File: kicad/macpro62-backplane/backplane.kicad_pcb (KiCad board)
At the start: 6 copper layers, 122 x 122 mm, 29 parts, among them J1 CPU-LINK: Amphenol Mini Cool 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, J10 MCIO 124 RA OUT -> Face S (x4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, J2 PSU-IN: Micro-Fit 3.0 2x4 (12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, J3 FACE-P AUX: JST GH 15P (MP62-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, J4 FACE-S AUX: JST GH 15P (same 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, J6 IOB-LINK: GH 15P <-> IOB J6 (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, J7 OpenCore boot: M.2 M-key sock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, J8 SWD (3V3, SWCLK, SWDIO, GND) 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, J9 MCIO 124 RA OUT -> Face P (x1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, SW1 BOOTSEL (fp5: PSU side), SW2 Bench power button, U1 RP2350A (LCSC C42411118), U10 OPTION Gen5: DS320PR810 #1, F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, U11 OPTION Gen5: DS320PR810 #2, F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, U12 OPTION Gen5: DS320PR810 #3, F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, U13 OPTION Gen5: DS320PR810 #4, F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, U14 OPTION Gen5: DS320PR810 #5, F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, U2 W25Q128 QSPI flash (part TBD), U3 TMP1075 core-base temp sensor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, U4 TMP1075 PSU-side temp sensor 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, Y1 12 MHz crystal

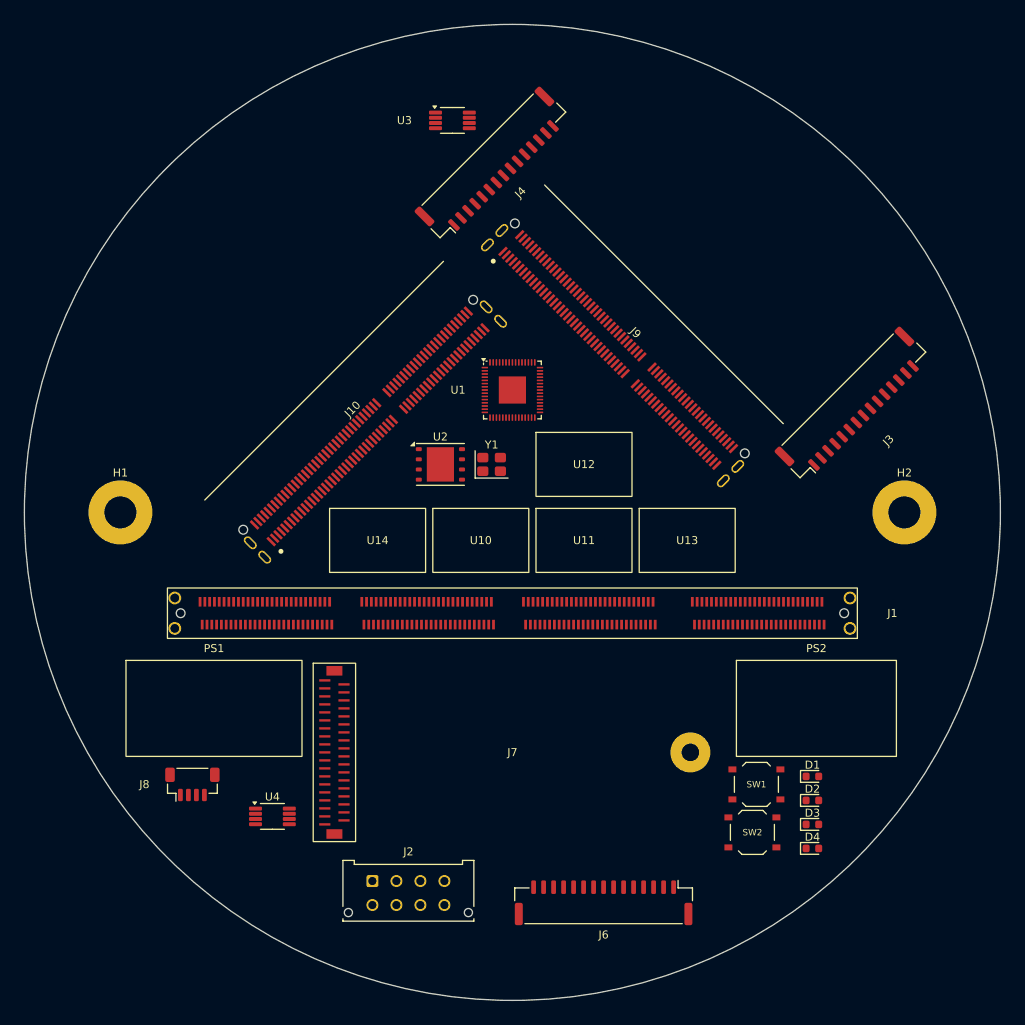
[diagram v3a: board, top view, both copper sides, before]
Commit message: Backplane rev A1: 4-layer JLC04161H-7628, Gen5 redrivers removed, RP2350B MCU + INA226, fully routed (DRC/ERC 0, all HS/SATA pairs 0 skew), USB2 skew touch-up, JLC outputs
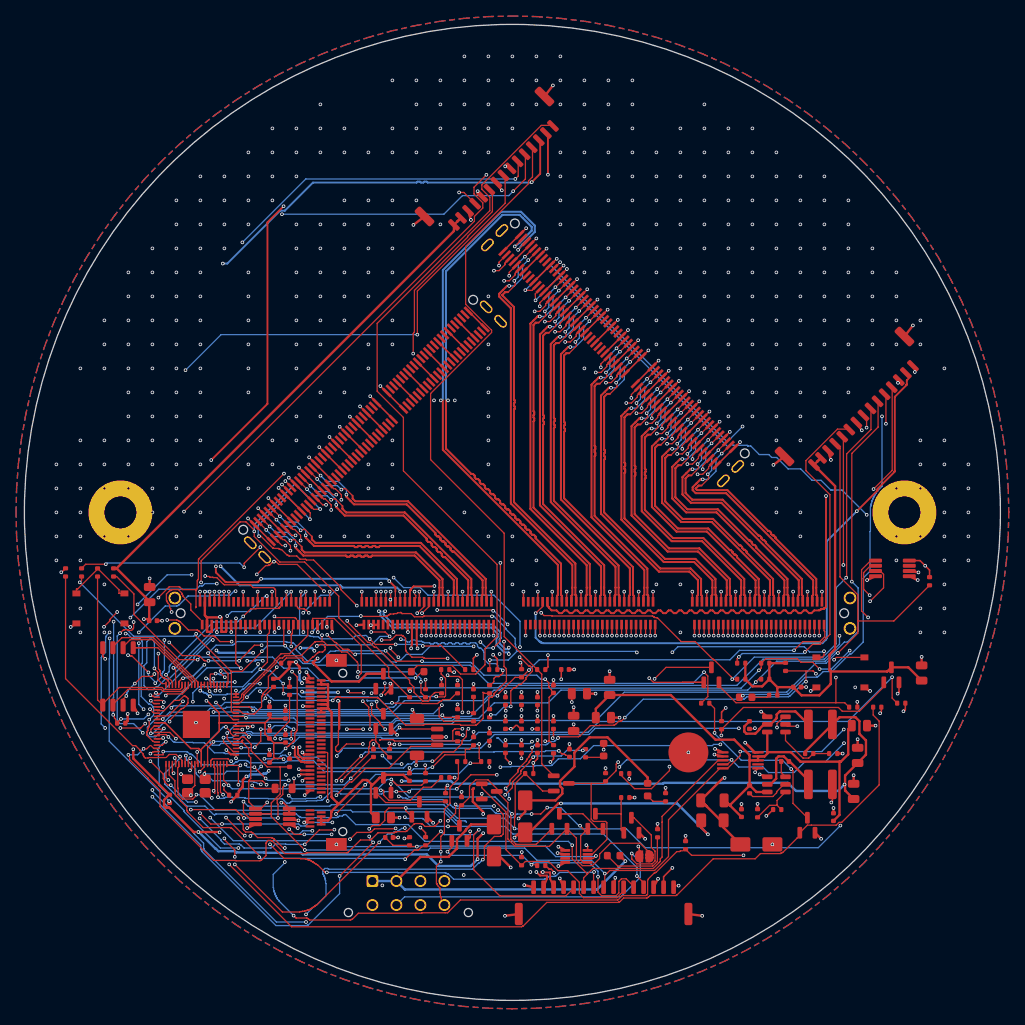
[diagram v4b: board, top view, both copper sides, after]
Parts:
- removed PS1: Standby power + HW safety gate, MP62_Placeholders:MP62_AREA_StandbyPower_22x12_PLACEHOLDER
- removed PS2: Main-rail power (3V3_BP incl. redrivers ~6.5 W), MP62_Placeholders:MP62_AREA_MainPower_20x12_PLACEHOLDER
- removed U10: OPTION Gen5: DS320PR810 #1, Face P lanes 0-3 (TX+RX), MP62_Placeholders:MP62_AREA_Redriver_DS320PR810_12x8_PLACEHOLDER
- removed U11: OPTION Gen5: DS320PR810 #2, Face P lanes 4-7 (TX+RX), MP62_Placeholders:MP62_AREA_Redriver_DS320PR810_12x8_PLACEHOLDER
- removed U12: OPTION Gen5: DS320PR810 #3, Face P lanes 8-11 (TX+RX), MP62_Placeholders:MP62_AREA_Redriver_DS320PR810_12x8_PLACEHOLDER
- removed U13: OPTION Gen5: DS320PR810 #4, Face P lanes 12-15 (TX+RX), MP62_Placeholders:MP62_AREA_Redriver_DS320PR810_12x8_PLACEHOLDER
- removed U14: OPTION Gen5: DS320PR810 #5, Face S lanes 0-3 (TX+RX), MP62_Placeholders:MP62_AREA_Redriver_DS320PR810_12x8_PLACEHOLDER
- added C1: 100nF 16V X7R 0402, MP62_BP:C_0402_1005Metric, F.Cu at (147.1, 128.1)
- added C10: 22uF 25V X5R 0805, MP62_BP:C_0805_2012Metric, F.Cu at (192.7, 134.9)
- added C11: 22uF 25V X5R 0805, MP62_BP:C_0805_2012Metric, F.Cu at (193.2, 130.4)
- added C12: 100nF 16V X7R 0402, MP62_BP:C_0402_1005Metric, F.Cu at (178.6, 137.6)
- added C13: 22uF 25V X5R 0805, MP62_BP:C_0805_2012Metric, F.Cu at (201.2, 120.1)
- added C14: 100nF 16V X7R 0402, MP62_BP:C_0402_1005Metric, F.Cu at (185.6, 121.8)
- added C15: 22uF 25V X5R 0805, MP62_BP:C_0805_2012Metric, F.Cu at (104.7, 110.3)
- added C16: 100nF 16V X7R 0402, MP62_BP:C_0402_1005Metric, F.Cu at (105.1, 113.5)
- added C17: 22uF 25V X5R 0805, MP62_BP:C_0805_2012Metric, F.Cu at (133.9, 138.2)
- added C18: 100nF 16V X7R 0402, MP62_BP:C_0402_1005Metric, F.Cu at (137.1, 133.1)
- added C19: 100nF 16V X7R 0402, MP62_BP:C_0402_1005Metric, F.Cu at (149.1, 126.6)
- added C2: 22uF 25V X5R 0805, MP62_BP:C_0805_2012Metric, F.Cu at (193.4, 126.7)
- added C20: 1uF 25V X5R 0402, MP62_BP:C_0402_1005Metric, F.Cu at (134.6, 140.6)
- added C21: 100nF 16V X7R 0402, MP62_BP:C_0402_1005Metric, F.Cu at (149.1, 123.6)
- added C22: 100nF 16V X7R 0402, MP62_BP:C_0402_1005Metric, F.Cu at (149.1, 129.6)
- added C23: 100nF 16V X7R 0402, MP62_BP:C_0402_1005Metric, F.Cu at (151.1, 126.6)
- added C24: 100nF 16V X7R 0402, MP62_BP:C_0402_1005Metric, F.Cu at (151.1, 123.6)
- added C25: 100nF 16V X7R 0402, MP62_BP:C_0402_1005Metric, F.Cu at (151.1, 129.6)
- added C26: 100nF 16V X7R 0402, MP62_BP:C_0402_1005Metric, F.Cu at (153.1, 126.6)
- added C27: 100nF 16V X7R 0402, MP62_BP:C_0402_1005Metric, F.Cu at (153.1, 123.6)
- added C28: 100nF 16V X7R 0402, MP62_BP:C_0402_1005Metric, F.Cu at (153.1, 129.6)
- added C29: 4.7uF 10V X5R 0402, MP62_BP:C_0402_1005Metric, F.Cu at (155.1, 126.6)
- added C3: 22uF 25V X5R 0805, MP62_BP:C_0805_2012Metric, F.Cu at (161.4, 125.7)
- added C30: 4.7uF 10V X5R 0402, MP62_BP:C_0402_1005Metric, F.Cu at (119.6, 127.8)
- added C31: 4.7uF 10V X5R 0402, MP62_BP:C_0402_1005Metric, F.Cu at (119.6, 130.8)
- added C32: 100nF 16V X7R 0402, MP62_BP:C_0402_1005Metric, F.Cu at (119.6, 124.8)
- added C33: 100nF 16V X7R 0402, MP62_BP:C_0402_1005Metric, F.Cu at (121.6, 128.3)
- added C34: 100nF 16V X7R 0402, MP62_BP:C_0402_1005Metric, F.Cu at (121.6, 125.3)
- added C35: 100nF 16V X7R 0402, MP62_BP:C_0402_1005Metric, F.Cu at (155.1, 122.1)
- added C36: 15pF 50V C0G 0402, MP62_BP:C_0402_1005Metric, F.Cu at (132.6, 130.1)
- added C37: 15pF 50V C0G 0402, MP62_BP:C_0402_1005Metric, F.Cu at (145.1, 122.6)
- added C38: 100nF 16V X7R 0402, MP62_BP:C_0402_1005Metric, F.Cu at (156.6, 119.6)
- added C39: 100nF 16V X7R 0402, MP62_BP:C_0402_1005Metric, F.Cu at (157.1, 130.1)
- added C4: 22uF 25V X5R 0805, MP62_BP:C_0805_2012Metric, F.Cu at (162.2, 121.9)
- added C5: 100nF 16V X7R 0402, MP62_BP:C_0402_1005Metric, F.Cu at (184.1, 131.1)
- added C6: 22uF 25V X5R 0805, MP62_BP:C_0805_2012Metric, F.Cu at (157.7, 126.4)
- added C7: 22uF 25V X5R 0805, MP62_BP:C_0805_2012Metric, F.Cu at (158.4, 122.7)
- added C8: 100nF 16V X7R 0402, MP62_BP:C_0402_1005Metric, F.Cu at (190.1, 138.1)
- added C9: 100nF 16V X7R 0402, MP62_BP:C_0402_1005Metric, F.Cu at (179.6, 126.6)
- added D10: LED red 0603, MP62_BP:LED_0603_1608Metric, F.Cu at (161.4, 129.7)
- added D5: BAT54A (LBAT54ALT1G), MP62_BP:SOT-23, F.Cu at (156.1, 133.9)
- added D6: LED red 0603, MP62_BP:LED_0603_1608Metric, F.Cu at (179.2, 123.1)
- added D7: LED red 0603, MP62_BP:LED_0603_1608Metric, F.Cu at (138.2, 119.9)
- added D8: LED red 0603, MP62_BP:LED_0603_1608Metric, F.Cu at (162.7, 142.9)
- added D9: LED red 0603, MP62_BP:LED_0603_1608Metric, F.Cu at (166.9, 134.7)
- added F1: 3A 1206 fast fuse (0466003.NRHF class), MP62_BP:Fuse_1206_3216Metric, F.Cu at (175.0, 138.5)
- added H3: M.2 2242 standoff pad (DNP option), MP62_BP:MP62_M2_Standoff_SMT_M2_Pad5.0, F.Cu at (172.0, 130.0)
- added JP1: BENCH: bridges the Hall interlock (open = normal), MP62_BP:SolderJumper-2_P1.3mm_Open_RoundedPad1.0x1.5mm, F.Cu at (166.5, 143.0)
- added L1: 4.7uH 2A 4x4 (SWPA4030S4R7MT), MP62_BP:L_Changjiang_FNR4030S, F.Cu at (188.5, 134.0)
- added L2: 4.7uH 2A 4x4 (SWPA4030S4R7MT), MP62_BP:L_Changjiang_FNR4030S, F.Cu at (188.5, 126.5)
- added L3: 3.3uH 0806 (FNR201610S3R3MT, RP2350 VREG), MP62_BP:L_0805_2012Metric, F.Cu at (121.4, 134.5)
- added Q1: AO3401A P-MOS, MP62_BP:SOT-23, F.Cu at (197.4, 120.3)
- added Q10: 2N7002 N-MOS, MP62_BP:SOT-23, F.Cu at (186.9, 139.1)
- added Q11: 2N7002 N-MOS, MP62_BP:SOT-23, F.Cu at (133.9, 126.1)
- added Q2: AO3401A P-MOS, MP62_BP:SOT-23, F.Cu at (133.9, 121.1)
- added Q3: AO3401A P-MOS, MP62_BP:SOT-23, F.Cu at (133.9, 134.1)
- added Q4: 2N7002 N-MOS, MP62_BP:SOT-23, F.Cu at (138.4, 137.1)
- added Q5: AO3401A P-MOS, MP62_BP:SOT-23, F.Cu at (143.4, 140.1)
- added Q6: AO3401A P-MOS, MP62_BP:SOT-23, F.Cu at (147.1, 134.9)
- added Q7: AO3401A P-MOS, MP62_BP:SOT-23, F.Cu at (155.9, 138.6)
- added Q8: AO3401A P-MOS, MP62_BP:SOT-23, F.Cu at (160.4, 138.6)
- added Q9: 2N7002 N-MOS, MP62_BP:SOT-23, F.Cu at (164.9, 139.1)
- added R1: 33k 1% 0402, MP62_BP:R_0402_1005Metric, F.Cu at (183.1, 137.1)
- added R10: 10k 1% 0402, MP62_BP:R_0402_1005Metric, F.Cu at (141.6, 133.1)
- added R100: 10mR 1% 1W 1206 shunt, MP62_BP:R_1206_3216Metric, F.Cu at (175.0, 136.0)
- added R11: 100k 1% 0402, MP62_BP:R_0402_1005Metric, F.Cu at (143.6, 136.1)
- added R12: 100k 1% 0402, MP62_BP:R_0402_1005Metric, F.Cu at (164.1, 135.6)
- added R13: 10k 1% 0402, MP62_BP:R_0402_1005Metric, F.Cu at (153.6, 144.1)
- added R14: 10k 1% 0402, MP62_BP:R_0402_1005Metric, F.Cu at (151.1, 143.6)
- added R15: 10k 1% 0402, MP62_BP:R_0402_1005Metric, F.Cu at (139.1, 133.1)
- added R16: 10k 1% 0402, MP62_BP:R_0402_1005Metric, F.Cu at (137.1, 141.1)
- added R17: 10k 1% 0402, MP62_BP:R_0402_1005Metric, F.Cu at (161.6, 133.1)
- added R18: 10k 1% 0402, MP62_BP:R_0402_1005Metric, F.Cu at (147.6, 119.6)
- added R19: 10k 1% 0402, MP62_BP:R_0402_1005Metric, F.Cu at (192.6, 124.3)
- added R2: 10k 1% 0402, MP62_BP:R_0402_1005Metric, F.Cu at (180.6, 137.6)
- added R20: 10k 1% 0402, MP62_BP:R_0402_1005Metric, F.Cu at (153.6, 119.6)
- added R21: 10k 1% 0402, MP62_BP:R_0402_1005Metric, F.Cu at (152.1, 132.6)
- added R22: 1k 1% 0402, MP62_BP:R_0402_1005Metric, F.Cu at (174.1, 123.8)
- added R23: 10k 1% 0402, MP62_BP:R_0402_1005Metric, F.Cu at (195.6, 124.3)
- added R24: 10k 1% 0402, MP62_BP:R_0402_1005Metric, F.Cu at (198.6, 123.8)
- added R25: 10k 1% 0402, MP62_BP:R_0402_1005Metric, F.Cu at (202.1, 108.6)
- added R26: 10k 1% 0402, MP62_BP:R_0402_1005Metric, F.Cu at (178.6, 118.8)
- added R27: 2.2k 1% 0402, MP62_BP:R_0402_1005Metric, F.Cu at (181.6, 118.8)
- added R28: 2.2k 1% 0402, MP62_BP:R_0402_1005Metric, F.Cu at (178.6, 120.8)
- added R29: 10k 1% 0402, MP62_BP:R_0402_1005Metric, F.Cu at (181.6, 120.8)
- added R3: 56k 1% 0402, MP62_BP:R_0402_1005Metric, F.Cu at (187.1, 130.1)
- added R30: 10k 1% 0402, MP62_BP:R_0402_1005Metric, F.Cu at (184.1, 119.3)
- added R31: 1k 1% 0402, MP62_BP:R_0402_1005Metric, F.Cu at (182.6, 122.8)
- added R32: 1k 1% 0402, MP62_BP:R_0402_1005Metric, F.Cu at (96.1, 107.5)
- added R33: 10k 1% 0402, MP62_BP:R_0402_1005Metric, F.Cu at (134.6, 130.1)
- added R34: 10k 1% 0402, MP62_BP:R_0402_1005Metric, F.Cu at (137.1, 122.6)
- added R35: 10k 1% 0402, MP62_BP:R_0402_1005Metric, F.Cu at (141.6, 119.6)
- added R36: 10k 1% 0402, MP62_BP:R_0402_1005Metric, F.Cu at (121.6, 118.8)
- added R37: 2.2k 1% 0402, MP62_BP:R_0402_1005Metric, F.Cu at (120.1, 121.3)
- added R38: 2.2k 1% 0402, MP62_BP:R_0402_1005Metric, F.Cu at (101.1, 126.3)
- added R39: 10k 1% 0402, MP62_BP:R_0402_1005Metric, F.Cu at (115.1, 135.3)
- added R4: 10k 1% 0402, MP62_BP:R_0402_1005Metric, F.Cu at (190.1, 130.1)
- added R40: 10k 1% 0402, MP62_BP:R_0402_1005Metric, F.Cu at (107.1, 135.8)
- added R41: 1k 1% 0402, MP62_BP:R_0402_1005Metric, F.Cu at (100.1, 107.5)
- added R42: 10k 1% 0402, MP62_BP:R_0402_1005Metric, F.Cu at (139.1, 122.6)
- added R43: 10k 1% 0402, MP62_BP:R_0402_1005Metric, F.Cu at (141.1, 122.1)
- added R44: 10k 1% 0402, MP62_BP:R_0402_1005Metric, F.Cu at (143.1, 122.1)
- added R45: 10k 1% 0402, MP62_BP:R_0402_1005Metric, F.Cu at (151.1, 120.1)
- added R46: 10k 1% 0402, MP62_BP:R_0402_1005Metric, F.Cu at (143.1, 125.1)
- added R47: 10k 1% 0402, MP62_BP:R_0402_1005Metric, F.Cu at (94.1, 107.5)
- added R48: 10k 1% 0402, MP62_BP:R_0402_1005Metric, F.Cu at (139.1, 141.1)
- added R49: 10k 1% 0402, MP62_BP:R_0402_1005Metric, F.Cu at (164.1, 132.6)
- added R5: 100k 1% 0402 (U6 EN, always on), MP62_BP:R_0402_1005Metric, F.Cu at (179.6, 134.6)
- added R50: 2.2k 1% 0402, MP62_BP:R_0402_1005Metric, F.Cu at (144.6, 119.6)
- added R51: 2.2k 1% 0402, MP62_BP:R_0402_1005Metric, F.Cu at (143.1, 128.1)
- added R52: 2.2k 1% 0402, MP62_BP:R_0402_1005Metric, F.Cu at (122.1, 131.3)
- added R53: 2.2k 1% 0402, MP62_BP:R_0402_1005Metric, F.Cu at (122.1, 122.3)
- added R54: 1k 1% 0402, MP62_BP:R_0402_1005Metric, F.Cu at (143.6, 131.1)
- added R55: 100k 1% 0402, MP62_BP:R_0402_1005Metric, F.Cu at (145.1, 128.6)
- added R56: 10k 1% 0402 (12V LED), MP62_BP:R_0402_1005Metric, F.Cu at (168.1, 140.1)
- added R57: 10k 1% 0402 (11V_SB LED), MP62_BP:R_0402_1005Metric, F.Cu at (169.1, 135.6)
- added R58: 1k 1% 0402, MP62_BP:R_0402_1005Metric, F.Cu at (159.1, 130.1)
- added R59: 33R 1% 0402, MP62_BP:R_0402_1005Metric, F.Cu at (155.1, 129.6)
- added R6: 100k 1% 0402 (U7 off until the MCU enables 5V_SBY), MP62_BP:R_0402_1005Metric, F.Cu at (171.6, 141.6)
- added R60: 1k 1% 0402, MP62_BP:R_0402_1005Metric, F.Cu at (145.1, 125.6)
- added R61: 1k 1% 0402, MP62_BP:R_0402_1005Metric, F.Cu at (98.1, 107.5)
- added R62: 33R 1% 0402, MP62_BP:R_0402_1005Metric, F.Cu at (147.1, 122.1)
- added R63: 33R 1% 0402, MP62_BP:R_0402_1005Metric, F.Cu at (147.1, 125.1)
- added R7: 10k 1% 0402, MP62_BP:R_0402_1005Metric, F.Cu at (176.1, 126.6)
- added R8: 10k 1% 0402, MP62_BP:R_0402_1005Metric, F.Cu at (146.6, 131.1)
- added R9: 10k 1% 0402, MP62_BP:R_0402_1005Metric, F.Cu at (141.6, 135.6)
- added U5: INA226AIDGSR @0x40 (C49851), MP62_BP:VSSOP-10_3x3mm_P0.5mm, F.Cu at (178.5, 131.0)
- added U6: TPS563201DDCR (C116592) -> 3V3_SB, MP62_BP:SOT-23-6, F.Cu at (183.0, 134.0)
- added U7: TPS563201DDCR (C116592) -> 5V_SBY, MP62_BP:SOT-23-6, F.Cu at (183.0, 126.5)
- added U8: SN74LVC1G74DCUR thermal latch (C70285), MP62_BP:VSSOP-8_2.3x2mm_P0.5mm, F.Cu at (158.0, 143.0)
- D1: value LED 11V_SB -> SS34 3A 40V Schottky SMA; footprint LED_SMD:LED_0603_1608Metric -> MP62_BP:D_SMA
- D2: value LED 12V main -> SS34 3A 40V Schottky SMA; footprint LED_SMD:LED_0603_1608Metric -> MP62_BP:D_SMA
- D3: value LED S0 -> SMAJ15A TVS SMA; footprint LED_SMD:LED_0603_1608Metric -> MP62_BP:D_SMA
- D4: value LED FAULT -> BAT54A (LBAT54ALT1G); footprint LED_SMD:LED_0603_1608Metric -> MP62_BP:SOT-23
- H1: value MountingHole D4 plated (stock D4.000 at x=-49) -> MountingHole D4 plated (GND); footprint MountingHole:MountingHole_4mm_Pad -> MP62_BP:MountingHole_4mm_Pad
- H2: value MountingHole D4 plated (stock D4.000 at x=+49) -> MountingHole D4 plated (GND); footprint MountingHole:MountingHole_4mm_Pad -> MP62_BP:MountingHole_4mm_Pad
- J1: value CPU-LINK: Amphenol Mini Cool Edge 224P vertical (ME1022410103011) at stock riser-slot position (ESTIMATE y=-12.6) -> ME1022410103011 Mini Cool Edge 224 (C4941560, 0 stock: pre-order); footprint MP62_Placeholders:MP62_CPULINK_MiniCoolEdge_224P_Vertical_SMT_PLACEHOLDER -> MP62_BP:MP62_CPULINK_MiniCoolEdge_224P_Vertical_SMT_PLACEHOLDER
- J10: value MCIO 124 RA OUT -> Face S (x4 wired, REFCLK, PERST#, sideband); cable exits radially under the Face S board edge -> MCIO 124P RA (C4867471) -> Face S x4; footprint MP62_Placeholders:MP62_MCIO_124P_RA_SFF-TA-1016 -> MP62_BP:MP62_MCIO_124P_RA_SFF-TA-1016
- J2: value PSU-IN: Micro-Fit 3.0 2x4 (12V x2, GND x3, 11V_SB, PS_ON#, PWR_OK) -> Molex 43045-0812 Micro-Fit 2x4 (C277661); footprint Connector_Molex:Molex_Micro-Fit_3.0_43045-0812_2x04_P3.00mm_Vertical -> MP62_BP:Molex_Micro-Fit_3.0_43045-0812_2x04_P3.00mm_Vertical
- J3: value FACE-P AUX: JST GH 15P (MP62-FACE v0.1 J_AUX: PWR_EN, PWR_GOOD, SMBus, THERM, PRSNT, 3V3_AUX, USB2, MOD_LED#) -> BM15B-GHS-TBT (C5305069) Face P AUX; footprint Connector_JST:JST_GH_BM15B-GHS-TBT_1x15-1MP_P1.25mm_Vertical -> MP62_BP:JST_GH_BM15B-GHS-TBT_1x15-1MP_P1.25mm_Vertical
- J4: value FACE-S AUX: JST GH 15P (same pinout as J3) -> BM15B-GHS-TBT (C5305069) Face S AUX; footprint Connector_JST:JST_GH_BM15B-GHS-TBT_1x15-1MP_P1.25mm_Vertical -> MP62_BP:JST_GH_BM15B-GHS-TBT_1x15-1MP_P1.25mm_Vertical
- J6: value IOB-LINK: GH 15P <-> IOB J6 (3V3_SB x2, PWRBTN_IN_N, HALL_A/B_N, I2C_SYS, IOB_INT_N, IOB_PRSNT_N, USB2_LINK, GND) -> BM15B-GHS-TBT (C5305069) IOB-LINK; footprint Connector_JST:JST_GH_BM15B-GHS-TBT_1x15-1MP_P1.25mm_Vertical -> MP62_BP:JST_GH_BM15B-GHS-TBT_1x15-1MP_P1.25mm_Vertical
- J7: value OpenCore boot: M.2 M-key socket, SATA0, 2242 card (PSU side; height under PSU TBD M7) -> M.2 M-key socket LOTES APCI0107 class (C841661) - DNP option (OpenCore boot SSD, SATA0); footprint MP62_Placeholders:MP62_M2_2242_MKey_SATA_PLACEHOLDER -> MP62_BP:MP62_M2_MKey_SMT_H4.2_PLACEHOLDER
- J8: value SWD (3V3, SWCLK, SWDIO, GND) (fp5: PSU side) -> BM03B-SRSS-TB SWD (DNP); footprint Connector_JST:JST_SH_BM04B-SRSS-TB_1x04-1MP_P1.00mm_Vertical -> MP62_BP:JST_SH_BM03B-SRSS-TB_1x03-1MP_P1.00mm_Vertical
- J9: value MCIO 124 RA OUT -> Face P (x16, REFCLK, PERST#, sideband); cable exits radially under the Face P board edge -> MCIO 124P RA G97R24332HR class (C4867471, 0 stock: pre-order) -> Face P x16; footprint MP62_Placeholders:MP62_MCIO_124P_RA_SFF-TA-1016 -> MP62_BP:MP62_MCIO_124P_RA_SFF-TA-1016
- SW1: value BOOTSEL (fp5: PSU side) -> BOOTSEL (TS-1187A); footprint Button_Switch_SMD:SW_Push_1P1T_XKB_TS-1187A -> MP62_BP:SW_Push_1P1T_XKB_TS-1187A
- SW2: value Bench power button -> BENCH power button (TS-1187A); footprint Button_Switch_SMD:SW_Push_1P1T_XKB_TS-1187A -> MP62_BP:SW_Push_1P1T_XKB_TS-1187A
- U1: value RP2350A (LCSC C42411118) -> RP2350B QFN-80 (C42415655); footprint Package_DFN_QFN:QFN-60-1EP_7x7mm_P0.4mm_EP3.4x3.4mm -> MP62_BP:QFN-80-1EP_10x10mm_P0.4mm_EP3.4x3.4mm
- U2: value W25Q128 QSPI flash (part TBD) -> W25Q128JVSIQ (C97521, basic); footprint Package_SON:WSON-8-1EP_6x5mm_P1.27mm_EP3.4x4.3mm -> MP62_BP:SOIC-8_5.3x5.3mm_P1.27mm
- U3: value TMP1075 core-base temp sensor #1 (under core bottom, I2C_SYS 0x48) -> TMP1075DGKR @0x48 core side (C2864807); footprint Package_SO:VSSOP-8_3x3mm_P0.65mm -> MP62_BP:VSSOP-8_3x3mm_P0.65mm
- U4: value TMP1075 PSU-side temp sensor #2 (I2C_SYS 0x49) -> TMP1075DGKR @0x49 PSU side (C2864807); footprint Package_SO:VSSOP-8_3x3mm_P0.65mm -> MP62_BP:VSSOP-8_3x3mm_P0.65mm
- Y1: value 12 MHz crystal -> 12MHz 3225 crystal 20pF; footprint Crystal:Crystal_SMD_3225-4Pin_3.2x2.5mm -> MP62_BP:Crystal_SMD_3225-4Pin_3.2x2.5mm
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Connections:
- D1 pad 1: (no net) -> VIN_OR
- D1 pad 2: (no net) -> 12V_MAIN_IN
- D2 pad 1: (no net) -> VIN_OR
- D2 pad 2: (no net) -> 11V_SB_IN
- D3 pad 1: (no net) -> VIN_F
- D3 pad 2: (no net) -> GND
- D4 pad 1: (no net) -> CB_THERMTRIP_N
- D4 pad 2: (no net) -> FP_THERM_TRIP_N
- H1 pad 1: (no net) -> GND
- H2 pad 1: (no net) -> GND
- J1 pad A1: (no net) -> CC_PRSNT1_N
- J1 pad A10: (no net) -> GND
- J1 pad A100: (no net) -> GND
- J1 pad A101: (no net) -> unconnected-(J1-BIOS_SEL-PadA101)
- J1 pad A102: (no net) -> unconnected-(J1-GPIO0-PadA102)
- J1 pad A103: (no net) -> GND
- J1 pad A104: (no net) -> unconnected-(J1-GPIO1-PadA104)
- J1 pad A105: (no net) -> CB_PWR_ALERT_N
- J1 pad A106: (no net) -> GND
- J1 pad A107: (no net) -> 5V_SBY
- J1 pad A108: (no net) -> 5V_SBY
- J1 pad A109: (no net) -> GND
- J1 pad A11: (no net) -> FP_TX12_P
- J1 pad A110: (no net) -> 5V_SBY
- J1 pad A111: (no net) -> 5V_SBY
- J1 pad A112: (no net) -> CC_PRSNT2_N
- J1 pad A12: (no net) -> FP_TX12_N
- J1 pad A13: (no net) -> GND
- J1 pad A14: (no net) -> FP_TX11_P
- J1 pad A15: (no net) -> FP_TX11_N
- J1 pad A16: (no net) -> GND
- J1 pad A17: (no net) -> FP_TX10_P
- J1 pad A18: (no net) -> FP_TX10_N
- J1 pad A19: (no net) -> GND
- J1 pad A2: (no net) -> FP_TX15_P
- J1 pad A20: (no net) -> FP_TX9_P
- J1 pad A21: (no net) -> FP_TX9_N
- J1 pad A22: (no net) -> GND
- J1 pad A23: (no net) -> FP_TX8_P
- J1 pad A24: (no net) -> FP_TX8_N
- J1 pad A25: (no net) -> GND
- J1 pad A26: (no net) -> FP_TX7_P
- J1 pad A27: (no net) -> FP_TX7_N
- J1 pad A28: (no net) -> GND
- J1 pad A29: (no net) -> GND
- J1 pad A3: (no net) -> FP_TX15_N
- J1 pad A30: (no net) -> FP_TX6_P
- J1 pad A31: (no net) -> FP_TX6_N
- J1 pad A32: (no net) -> GND
- J1 pad A33: (no net) -> FP_TX5_P
- J1 pad A34: (no net) -> FP_TX5_N
- J1 pad A35: (no net) -> GND
- J1 pad A36: (no net) -> FP_TX4_P
- J1 pad A37: (no net) -> FP_TX4_N
- J1 pad A38: (no net) -> GND
- J1 pad A39: (no net) -> FP_TX3_P
- J1 pad A4: (no net) -> GND
- J1 pad A40: (no net) -> FP_TX3_N
- J1 pad A41: (no net) -> GND
- J1 pad A42: (no net) -> FP_TX2_P
- J1 pad A43: (no net) -> FP_TX2_N
- J1 pad A44: (no net) -> GND
- J1 pad A45: (no net) -> FP_TX1_P
- J1 pad A46: (no net) -> FP_TX1_N
- J1 pad A47: (no net) -> GND
- J1 pad A48: (no net) -> FP_TX0_P
- J1 pad A49: (no net) -> FP_TX0_N
- J1 pad A5: (no net) -> FP_TX14_P
- J1 pad A50: (no net) -> GND
- J1 pad A51: (no net) -> FP_REFCLK_P
- J1 pad A52: (no net) -> FP_REFCLK_N
- J1 pad A53: (no net) -> GND
- J1 pad A54: (no net) -> unconnected-(J1-RSVD_REFCLK2_P-PadA54)
- J1 pad A55: (no net) -> unconnected-(J1-RSVD_REFCLK2_N-PadA55)
- J1 pad A56: (no net) -> GND
- J1 pad A57: (no net) -> GND
- J1 pad A58: (no net) -> FS_TX3_P
- J1 pad A59: (no net) -> FS_TX3_N
- J1 pad A6: (no net) -> FP_TX14_N
- J1 pad A60: (no net) -> GND
- J1 pad A61: (no net) -> FS_TX2_P
- J1 pad A62: (no net) -> FS_TX2_N
- J1 pad A63: (no net) -> GND
- J1 pad A64: (no net) -> FS_TX1_P
- J1 pad A65: (no net) -> FS_TX1_N
- J1 pad A66: (no net) -> GND
- J1 pad A67: (no net) -> FS_TX0_P
- J1 pad A68: (no net) -> FS_TX0_N
- J1 pad A69: (no net) -> GND
- J1 pad A7: (no net) -> GND
- J1 pad A70: (no net) -> FS_REFCLK_P
- J1 pad A71: (no net) -> FS_REFCLK_N
- J1 pad A72: (no net) -> GND
- J1 pad A73: (no net) -> SATA0_TX_P
- J1 pad A74: (no net) -> SATA0_TX_N
- J1 pad A75: (no net) -> GND
- J1 pad A76: (no net) -> unconnected-(J1-RSVD_HS_A1_P-PadA76)
- J1 pad A77: (no net) -> unconnected-(J1-RSVD_HS_A1_N-PadA77)
- J1 pad A78: (no net) -> GND
- J1 pad A79: (no net) -> unconnected-(J1-RSVD_HS_A2_P-PadA79)
- J1 pad A8: (no net) -> FP_TX13_P
- J1 pad A80: (no net) -> unconnected-(J1-RSVD_HS_A2_N-PadA80)
- J1 pad A81: (no net) -> GND
- J1 pad A82: (no net) -> GND
- J1 pad A83: (no net) -> GND
- J1 pad A84: (no net) -> GND
- J1 pad A85: (no net) -> GND
- J1 pad A86: (no net) -> CB_PWRBTN_N
- J1 pad A87: (no net) -> unconnected-(J1-RSTBTN#-PadA87)
- J1 pad A88: (no net) -> GND
- J1 pad A89: (no net) -> CB_SUS_S3_N
- J1 pad A9: (no net) -> FP_TX13_N
- J1 pad A90: (no net) -> CB_SUS_S45_N
- J1 pad A91: (no net) -> GND
- J1 pad A92: (no net) -> CB_RSMRST_N
- J1 pad A93: (no net) -> CB_VIN_PWR_OK
- J1 pad A94: (no net) -> GND
- J1 pad A95: (no net) -> CB_PLTRST_N
- J1 pad A96: (no net) -> CB_THERMTRIP_N
- J1 pad A97: (no net) -> GND
- J1 pad A98: (no net) -> CB_CARRIER_HOT_N
- J1 pad A99: (no net) -> unconnected-(J1-WAKE0#-PadA99)
- J1 pad B1: (no net) -> GND
- J1 pad B10: (no net) -> GND
- J1 pad B100: (no net) -> GND
- J1 pad B101: (no net) -> unconnected-(J1-GPIO3-PadB101)
- J1 pad B102: (no net) -> unconnected-(J1-RSVD_LS2-PadB102)
- J1 pad B103: (no net) -> GND
- J1 pad B104: (no net) -> unconnected-(J1-RSVD_LS3-PadB104)
- J1 pad B105: (no net) -> unconnected-(J1-RSVD_LS4-PadB105)
- J1 pad B106: (no net) -> GND
- J1 pad B107: (no net) -> 3V3_SB
- J1 pad B108: (no net) -> 3V3_SB
- J1 pad B109: (no net) -> GND
- J1 pad B11: (no net) -> FP_RX12_P
- J1 pad B110: (no net) -> 5V_SBY
- J1 pad B111: (no net) -> 5V_SBY
- J1 pad B112: (no net) -> GND
- J1 pad B12: (no net) -> FP_RX12_N
- J1 pad B13: (no net) -> GND
- J1 pad B14: (no net) -> FP_RX11_P
- J1 pad B15: (no net) -> FP_RX11_N
- J1 pad B16: (no net) -> GND
- J1 pad B17: (no net) -> FP_RX10_P
- J1 pad B18: (no net) -> FP_RX10_N
- J1 pad B19: (no net) -> GND
- J1 pad B2: (no net) -> FP_RX15_P
- J1 pad B20: (no net) -> FP_RX9_P
- J1 pad B21: (no net) -> FP_RX9_N
- J1 pad B22: (no net) -> GND
- J1 pad B23: (no net) -> FP_RX8_P
- J1 pad B24: (no net) -> FP_RX8_N
- J1 pad B25: (no net) -> GND
- J1 pad B26: (no net) -> FP_RX7_P
- J1 pad B27: (no net) -> FP_RX7_N
- J1 pad B28: (no net) -> GND
- J1 pad B29: (no net) -> GND
- J1 pad B3: (no net) -> FP_RX15_N
- J1 pad B30: (no net) -> FP_RX6_P
- J1 pad B31: (no net) -> FP_RX6_N
- J1 pad B32: (no net) -> GND
- J1 pad B33: (no net) -> FP_RX5_P
- J1 pad B34: (no net) -> FP_RX5_N
- J1 pad B35: (no net) -> GND
- J1 pad B36: (no net) -> FP_RX4_P
- J1 pad B37: (no net) -> FP_RX4_N
- J1 pad B38: (no net) -> GND
- J1 pad B39: (no net) -> FP_RX3_P
- J1 pad B4: (no net) -> GND
- J1 pad B40: (no net) -> FP_RX3_N
- J1 pad B41: (no net) -> GND
- J1 pad B42: (no net) -> FP_RX2_P
- J1 pad B43: (no net) -> FP_RX2_N
- J1 pad B44: (no net) -> GND
- J1 pad B45: (no net) -> FP_RX1_P
- J1 pad B46: (no net) -> FP_RX1_N
- J1 pad B47: (no net) -> GND
- J1 pad B48: (no net) -> FP_RX0_P
- J1 pad B49: (no net) -> FP_RX0_N
- J1 pad B5: (no net) -> FP_RX14_P
- J1 pad B50: (no net) -> GND
- J1 pad B51: (no net) -> USB2_FACEP_P
- J1 pad B52: (no net) -> USB2_FACEP_N
- J1 pad B53: (no net) -> GND
- J1 pad B54: (no net) -> unconnected-(J1-RSVD_HS_B1_P-PadB54)
- J1 pad B55: (no net) -> unconnected-(J1-RSVD_HS_B1_N-PadB55)
- J1 pad B56: (no net) -> GND
- J1 pad B57: (no net) -> GND
- J1 pad B58: (no net) -> FS_RX3_P
- J1 pad B59: (no net) -> FS_RX3_N
- J1 pad B6: (no net) -> FP_RX14_N
- J1 pad B60: (no net) -> GND
- J1 pad B61: (no net) -> FS_RX2_P
- J1 pad B62: (no net) -> FS_RX2_N
- J1 pad B63: (no net) -> GND
- J1 pad B64: (no net) -> FS_RX1_P
- J1 pad B65: (no net) -> FS_RX1_N
- J1 pad B66: (no net) -> GND
- J1 pad B67: (no net) -> FS_RX0_P
- J1 pad B68: (no net) -> FS_RX0_N
- J1 pad B69: (no net) -> GND
- J1 pad B7: (no net) -> GND
- J1 pad B70: (no net) -> SATA0_RX_P
- J1 pad B71: (no net) -> SATA0_RX_N
- J1 pad B72: (no net) -> GND
- J1 pad B73: (no net) -> USB2_MCU_P
- J1 pad B74: (no net) -> USB2_MCU_N
- J1 pad B75: (no net) -> GND
- J1 pad B76: (no net) -> USB2_FACES_P
- J1 pad B77: (no net) -> USB2_FACES_N
- J1 pad B78: (no net) -> GND
- J1 pad B79: (no net) -> USB2_SPARE_P
- J1 pad B8: (no net) -> FP_RX13_P
- J1 pad B80: (no net) -> USB2_SPARE_N
- J1 pad B81: (no net) -> GND
- J1 pad B82: (no net) -> unconnected-(J1-RSVD_HS_B2_P-PadB82)
- J1 pad B83: (no net) -> unconnected-(J1-RSVD_HS_B2_N-PadB83)
- J1 pad B84: (no net) -> GND
- J1 pad B85: (no net) -> GND
- J1 pad B86: (no net) -> unconnected-(J1-SMB_CLK-PadB86)
- J1 pad B87: (no net) -> unconnected-(J1-SMB_DAT-PadB87)
- J1 pad B88: (no net) -> GND
- J1 pad B89: (no net) -> unconnected-(J1-SMB_ALERT#-PadB89)
- J1 pad B9: (no net) -> FP_RX13_N
- J1 pad B90: (no net) -> CB_I2C0_SCL
- J1 pad B91: (no net) -> GND
- J1 pad B92: (no net) -> CB_I2C0_SDA
- J1 pad B93: (no net) -> CB_UART0_TX
- J1 pad B94: (no net) -> GND
- J1 pad B95: (no net) -> CB_UART0_RX
- J1 pad B96: (no net) -> CB_FAN_PWM
- J1 pad B97: (no net) -> GND
- J1 pad B98: (no net) -> CB_FAN_TACH
- J1 pad B99: (no net) -> unconnected-(J1-GPIO2-PadB99)
- J1 pad BL: (no net) -> GND
- J10 pad A1: (no net) -> GND
- J10 pad A10: (no net) -> GND
- J10 pad A11: (no net) -> FS_REFCLK_P
- J10 pad A12: (no net) -> FS_REFCLK_N
- J10 pad A13: (no net) -> GND
- J10 pad A14: (no net) -> FS_RX2_P
- J10 pad A15: (no net) -> FS_RX2_N
- J10 pad A16: (no net) -> GND
- J10 pad A17: (no net) -> FS_RX3_P
- J10 pad A18: (no net) -> FS_RX3_N
- J10 pad A19: (no net) -> GND
- J10 pad A2: (no net) -> FS_RX0_P
- J10 pad A20: (no net) -> unconnected-(J10-PER4P-PadA20)
- J10 pad A21: (no net) -> unconnected-(J10-PER4N-PadA21)
- J10 pad A22: (no net) -> GND
- J10 pad A23: (no net) -> unconnected-(J10-PER5P-PadA23)
- J10 pad A24: (no net) -> unconnected-(J10-PER5N-PadA24)
- J10 pad A25: (no net) -> GND
- J10 pad A26: (no net) -> unconnected-(J10-RSVD-PadA26)
- J10 pad A27: (no net) -> unconnected-(J10-RSVD-PadA27)
- J10 pad A28: (no net) -> GND
- J10 pad A29: (no net) -> unconnected-(J10-RSVD-PadA29)
- J10 pad A3: (no net) -> FS_RX0_N
- J10 pad A30: (no net) -> unconnected-(J10-RSVD-PadA30)
- J10 pad A31: (no net) -> GND
- J10 pad A32: (no net) -> unconnected-(J10-PER6P-PadA32)
- J10 pad A33: (no net) -> unconnected-(J10-PER6N-PadA33)
- J10 pad A34: (no net) -> GND
- J10 pad A35: (no net) -> unconnected-(J10-PER7P-PadA35)
- J10 pad A36: (no net) -> unconnected-(J10-PER7N-PadA36)
- J10 pad A37: (no net) -> GND
- J10 pad A38: (no net) -> GND
- J10 pad A39: (no net) -> unconnected-(J10-PER8P-PadA39)
- J10 pad A4: (no net) -> GND
- J10 pad A40: (no net) -> unconnected-(J10-PER8N-PadA40)
- J10 pad A41: (no net) -> GND
- J10 pad A42: (no net) -> unconnected-(J10-PER9P-PadA42)
- J10 pad A43: (no net) -> unconnected-(J10-PER9N-PadA43)
- J10 pad A44: (no net) -> GND
- J10 pad A45: (no net) -> unconnected-(J10-PER10P-PadA45)
- J10 pad A46: (no net) -> unconnected-(J10-PER10N-PadA46)
- J10 pad A47: (no net) -> GND
- J10 pad A48: (no net) -> unconnected-(J10-PER11P-PadA48)
- J10 pad A49: (no net) -> unconnected-(J10-PER11N-PadA49)
- J10 pad A5: (no net) -> FS_RX1_P
- J10 pad A50: (no net) -> GND
- J10 pad A51: (no net) -> unconnected-(J10-PER12P-PadA51)
- J10 pad A52: (no net) -> unconnected-(J10-PER12N-PadA52)
- J10 pad A53: (no net) -> GND
- J10 pad A54: (no net) -> unconnected-(J10-PER13P-PadA54)
- J10 pad A55: (no net) -> unconnected-(J10-PER13N-PadA55)
- J10 pad A56: (no net) -> GND
- J10 pad A57: (no net) -> unconnected-(J10-PER14P-PadA57)
- J10 pad A58: (no net) -> unconnected-(J10-PER14N-PadA58)
- J10 pad A59: (no net) -> GND
- J10 pad A6: (no net) -> FS_RX1_N
- J10 pad A60: (no net) -> unconnected-(J10-PER15P-PadA60)
- J10 pad A61: (no net) -> unconnected-(J10-PER15N-PadA61)
- J10 pad A62: (no net) -> GND
- J10 pad A7: (no net) -> GND
- J10 pad A8: (no net) -> unconnected-(J10-CLKREQ-PadA8)
- J10 pad A9: (no net) -> unconnected-(J10-WAKE-PadA9)
- J10 pad B1: (no net) -> GND
- J10 pad B10: (no net) -> GND
- J10 pad B11: (no net) -> FS_PERST_N
- J10 pad B12: (no net) -> FS_MCIO_PRSNT_N
- J10 pad B13: (no net) -> GND
- J10 pad B14: (no net) -> FS_TX2_P
- J10 pad B15: (no net) -> FS_TX2_N
- J10 pad B16: (no net) -> GND
- J10 pad B17: (no net) -> FS_TX3_P
- J10 pad B18: (no net) -> FS_TX3_N
- J10 pad B19: (no net) -> GND
- J10 pad B2: (no net) -> FS_TX0_P
- J10 pad B20: (no net) -> unconnected-(J10-PET4P-PadB20)
- J10 pad B21: (no net) -> unconnected-(J10-PET4N-PadB21)
- J10 pad B22: (no net) -> GND
- J10 pad B23: (no net) -> unconnected-(J10-PET5P-PadB23)
- J10 pad B24: (no net) -> unconnected-(J10-PET5N-PadB24)
- J10 pad B25: (no net) -> GND
- J10 pad B26: (no net) -> unconnected-(J10-RSVD-PadB26)
- J10 pad B27: (no net) -> unconnected-(J10-RSVD-PadB27)
- J10 pad B28: (no net) -> GND
- J10 pad B29: (no net) -> unconnected-(J10-RSVD-PadB29)
- J10 pad B3: (no net) -> FS_TX0_N
- J10 pad B30: (no net) -> unconnected-(J10-RSVD-PadB30)
- J10 pad B31: (no net) -> GND
- J10 pad B32: (no net) -> unconnected-(J10-PET6P-PadB32)
- J10 pad B33: (no net) -> unconnected-(J10-PET6N-PadB33)
- J10 pad B34: (no net) -> GND
- J10 pad B35: (no net) -> unconnected-(J10-PET7P-PadB35)
- J10 pad B36: (no net) -> unconnected-(J10-PET7N-PadB36)
- J10 pad B37: (no net) -> GND
- J10 pad B38: (no net) -> GND
- J10 pad B39: (no net) -> unconnected-(J10-PET8P-PadB39)
- J10 pad B4: (no net) -> GND
- J10 pad B40: (no net) -> unconnected-(J10-PET8N-PadB40)
- J10 pad B41: (no net) -> GND
- J10 pad B42: (no net) -> unconnected-(J10-PET9P-PadB42)
- J10 pad B43: (no net) -> unconnected-(J10-PET9N-PadB43)
- J10 pad B44: (no net) -> GND
- J10 pad B45: (no net) -> unconnected-(J10-PET10P-PadB45)
- J10 pad B46: (no net) -> unconnected-(J10-PET10N-PadB46)
- J10 pad B47: (no net) -> GND
- J10 pad B48: (no net) -> unconnected-(J10-PET11P-PadB48)
- J10 pad B49: (no net) -> unconnected-(J10-PET11N-PadB49)
- J10 pad B5: (no net) -> FS_TX1_P
- J10 pad B50: (no net) -> GND
- J10 pad B51: (no net) -> unconnected-(J10-PET12P-PadB51)
- J10 pad B52: (no net) -> unconnected-(J10-PET12N-PadB52)
- J10 pad B53: (no net) -> GND
- J10 pad B54: (no net) -> unconnected-(J10-PET13P-PadB54)
- J10 pad B55: (no net) -> unconnected-(J10-PET13N-PadB55)
- J10 pad B56: (no net) -> GND
- J10 pad B57: (no net) -> unconnected-(J10-PET14P-PadB57)
- J10 pad B58: (no net) -> unconnected-(J10-PET14N-PadB58)
- J10 pad B59: (no net) -> GND
- J10 pad B6: (no net) -> FS_TX1_N
- J10 pad B60: (no net) -> unconnected-(J10-PET15P-PadB60)
- J10 pad B61: (no net) -> unconnected-(J10-PET15N-PadB61)
- J10 pad B62: (no net) -> GND
- J10 pad B7: (no net) -> GND
- J10 pad B8: (no net) -> unconnected-(J10-SMCLK-PadB8)
- J10 pad B9: (no net) -> unconnected-(J10-SMDAT-PadB9)
- J10 pad MP: (no net) -> GND
- J2 pad 1: (no net) -> 12V_MAIN_IN
- J2 pad 2: (no net) -> 12V_MAIN_IN
- J2 pad 3: (no net) -> GND
- J2 pad 4: (no net) -> GND
- J2 pad 5: (no net) -> GND
- J2 pad 6: (no net) -> PSU_PS_ON_N
- J2 pad 7: (no net) -> 11V_SB_IN
- J2 pad 8: (no net) -> PSU_PWR_OK
- J3 pad 1: (no net) -> 3V3_AUX_P
- J3 pad 10: (no net) -> FP_SMB_ALERT_N
- J3 pad 11: (no net) -> FP_THERM_ALERT_N
- J3 pad 12: (no net) -> FP_THERM_TRIP_N
- J3 pad 13: (no net) -> USB2_FACEP_P
- J3 pad 14: (no net) -> USB2_FACEP_N
- J3 pad 15: (no net) -> FP_MOD_LED_N
- J3 pad 2: (no net) -> 3V3_AUX_P
- J3 pad 3: (no net) -> GND
- J3 pad 4: (no net) -> FP_PRSNT_N
- J3 pad 5: (no net) -> FP_PWR_EN
- J3 pad 6: (no net) -> FP_PWR_GOOD
- J3 pad 7: (no net) -> GND
- J3 pad 8: (no net) -> FP_SMB_SCL
- J3 pad 9: (no net) -> FP_SMB_SDA
- J3 pad MP: (no net) -> GND
- J4 pad 1: (no net) -> 3V3_AUX_S
- J4 pad 10: (no net) -> FS_SMB_ALERT_N
- J4 pad 11: (no net) -> FS_THERM_ALERT_N
- J4 pad 12: (no net) -> FS_THERM_TRIP_N
- J4 pad 13: (no net) -> USB2_FACES_P
- J4 pad 14: (no net) -> USB2_FACES_N
- J4 pad 15: (no net) -> FS_MOD_LED_N
- J4 pad 2: (no net) -> 3V3_AUX_S
- J4 pad 3: (no net) -> GND
- J4 pad 4: (no net) -> FS_PRSNT_N
- J4 pad 5: (no net) -> FS_PWR_EN
- J4 pad 6: (no net) -> FS_PWR_GOOD
- J4 pad 7: (no net) -> GND
- J4 pad 8: (no net) -> FS_SMB_SCL
- J4 pad 9: (no net) -> FS_SMB_SDA
- J4 pad MP: (no net) -> GND
- J6 pad 1: (no net) -> 3V3_SB
- J6 pad 10: (no net) -> SYS_INT_N
- J6 pad 11: (no net) -> IOB_PRSNT_N
- J6 pad 12: (no net) -> GND
- J6 pad 13: (no net) -> USB2_SPARE_P
- J6 pad 14: (no net) -> USB2_SPARE_N
- J6 pad 15: (no net) -> GND
- J6 pad 2: (no net) -> 3V3_SB
- J6 pad 3: (no net) -> GND
- J6 pad 4: (no net) -> PWRBTN_IN_N
- J6 pad 5: (no net) -> HALL_A_N
- J6 pad 6: (no net) -> HALL_B_N
- J6 pad 7: (no net) -> GND
- J6 pad 8: (no net) -> I2C_SYS_SCL
- J6 pad 9: (no net) -> I2C_SYS_SDA
- J6 pad MP: (no net) -> GND
- J7 pad 1: (no net) -> GND
- J7 pad 10: (no net) -> unconnected-(J7-NC10-Pad10)
- J7 pad 11: (no net) -> unconnected-(J7-NC11-Pad11)
- J7 pad 12: (no net) -> 3V3_M2
- J7 pad 13: (no net) -> unconnected-(J7-NC13-Pad13)
- J7 pad 14: (no net) -> 3V3_M2
- J7 pad 15: (no net) -> GND
- J7 pad 16: (no net) -> 3V3_M2
- J7 pad 17: (no net) -> unconnected-(J7-NC17-Pad17)
- J7 pad 18: (no net) -> 3V3_M2
- J7 pad 19: (no net) -> unconnected-(J7-NC19-Pad19)
- J7 pad 2: (no net) -> 3V3_M2
- J7 pad 20: (no net) -> unconnected-(J7-NC20-Pad20)
- J7 pad 21: (no net) -> GND
- J7 pad 22: (no net) -> unconnected-(J7-NC22-Pad22)
- J7 pad 23: (no net) -> unconnected-(J7-NC23-Pad23)
- J7 pad 24: (no net) -> unconnected-(J7-NC24-Pad24)
- J7 pad 25: (no net) -> unconnected-(J7-NC25-Pad25)
- J7 pad 26: (no net) -> unconnected-(J7-NC26-Pad26)
- J7 pad 27: (no net) -> GND
- J7 pad 28: (no net) -> unconnected-(J7-NC28-Pad28)
- J7 pad 29: (no net) -> unconnected-(J7-NC29-Pad29)
- J7 pad 3: (no net) -> GND
- J7 pad 30: (no net) -> unconnected-(J7-NC30-Pad30)
- J7 pad 31: (no net) -> unconnected-(J7-NC31-Pad31)
- J7 pad 32: (no net) -> unconnected-(J7-NC32-Pad32)
- J7 pad 33: (no net) -> GND
- J7 pad 34: (no net) -> unconnected-(J7-NC34-Pad34)
- J7 pad 35: (no net) -> unconnected-(J7-NC35-Pad35)
- J7 pad 36: (no net) -> unconnected-(J7-NC36-Pad36)
- J7 pad 37: (no net) -> unconnected-(J7-NC37-Pad37)
- J7 pad 4: (no net) -> 3V3_M2
- J7 pad 5: (no net) -> unconnected-(J7-NC5-Pad5)
- J7 pad 6: (no net) -> unconnected-(J7-NC6-Pad6)
- J7 pad 7: (no net) -> unconnected-(J7-NC7-Pad7)
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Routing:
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- added copper zone on In2.Cu, net 3V3_SB
- added copper zone on B.Cu, net GND
- added copper zone on F.Cu, net GND
- added copper zone on In1.Cu, net GND
- added copper zone on In2.Cu, net GND
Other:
- copper layers 6 -> 4
- board text added: "MP62 BP rev A1 'BP-G4' (4 layers, Gen4, RP2350B). Not for fab before the ICD rev 3.1 FS-lane decision"
- board text removed: "12 V main to CPU board and faces: bus bars / lugs, NOT through the edge."
- board text removed: "COMPONENT KEEP-OUT RING 3 mm (R58-R61): chassis fillet + standoff margin. Height limit inside R58 TBD (measure core-to-base gap)"
- board text removed: "CPU board plane (slot measured -12.5 +/- 0.3 on the scan, M2b)"
- board text removed: "CPU carrier 224 card (79.89 x 1.57) enters J1 here (J1 at 180 deg: A row = host TX on the PSU side, A1 at +x); parts within ~6 mm: height <= shoulder gap (M3)"
- board text removed: "Disc D122 (Fusion base_board_outline.dxf), holes D4 at (+/-49, 0)"
- board text removed: "Face P board plane ~55 mm (M2) at 45 deg (M2c, Aidan ~45), bottom edge ~15 mm above BP (M1)"
- board text removed: "Face P x16 corridor (TX L1 / RX L6)"
- board text removed: "Face S board plane ~55 mm (M2) at 135 deg (M2c, Aidan ~45), bottom edge ~15 mm above BP (M1)"
- board text removed: "Face S x4 corridor"
- board text removed: "J1 = CPU-LINK: Amphenol Mini Cool Edge 224 vertical; CPU board card edge (1.57 mm), MP62 pinout."
- board text removed: "J_PCIE (module X 47.0, s=+5.0); BP receptacle s=+5.0 -> cable jog 0.0 mm (zero, O-10)"
- board text removed: "MCIO ribbon corridor (no parts): narrow straight plug (<= 10.0 high) ends n 41.5; ribbon ~10 mm under the 15 mm board edge, bends up outside (R >= 3), jog 0.0"
- board text removed: "MCIO ribbon corridor (no parts): narrow straight plug (<= 10.0 high) ends n 45.0; ribbon ~10 mm under the 15 mm board edge, bends up outside (R >= 3), jog 0.0"
- board text removed: "MP62 BACKPLANE rev A - FIRST-PASS FLOORPLAN, HUB TOPOLOGY (not routed)"
- board text removed: "No AC caps on BP: host-TX caps on module/CPU board, device-TX caps on face module."
- board text removed: "PCIe: J1 -> (opt. DS320PR810 x5) -> J9 MCIO 124 Face P x16 / J10 MCIO 124 Face S x4 (AUX: J3 / J4)."
- board text removed: "PSU SIDE (behind CPU board, under PSU): heights TBD (M7)"
- board text removed: "S1 stock hole: D6 keep-out (CR-BP-1)"
- board text removed: "S2 stock hole: D6 keep-out (CR-BP-1)"
- board text removed: "S3 stock hole: D6 keep-out (CR-BP-1)"
- board text removed: "S4 stock hole: D6 keep-out (CR-BP-1)"
- board text removed: "S5 stock hole: D6 keep-out (CR-BP-1)"
- board text removed: "S6 stock hole: D6 keep-out (CR-BP-1)"
- board text removed: "fp6 (ICD O-10): J9/J10 land at s = +5.0 = module J_PCIE X 47.0 (zero jog); straight-straight MCIO 124 cable, NARROW plugs."
- board text removed: "open core interior / air path above the region bounded by the 3 board planes (45/135 deg: incentre (0, 24.8), inradius ~37; disc centre 12.6 mm inside the CPU board)"
